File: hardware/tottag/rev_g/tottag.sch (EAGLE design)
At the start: 193 parts, among them J1 USB4110-GF-A, J2 DM3AT-SF-PEJM5, J3 TC2030-JLINK-NL-2SIDE, J4 TC2030-JLINK-NL-2SIDE, J5 MOLEX-PICO-SPOX-3SIDE, Q1 CSD75207W15, Q4 CSD75207W15, T1 HHM1595A1, U1 DW1000, U10 STM32F091CC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

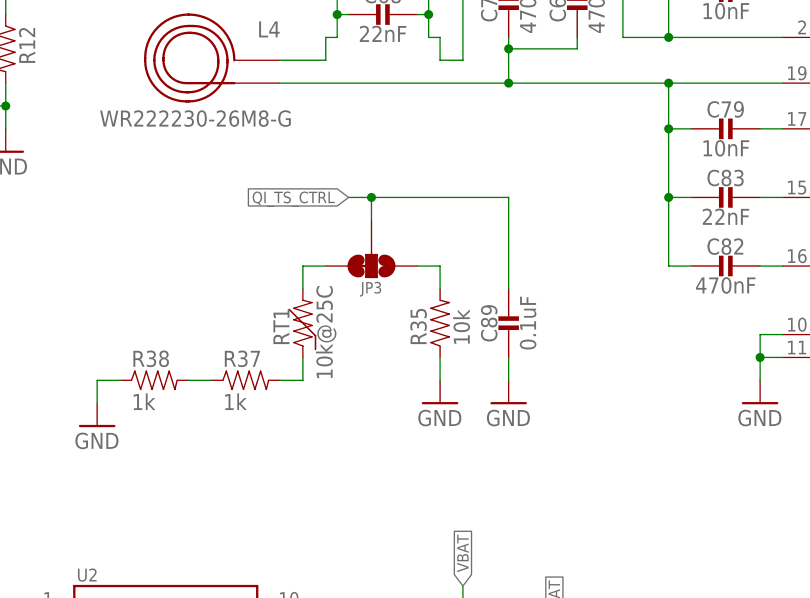
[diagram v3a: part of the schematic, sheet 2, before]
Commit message: rev_g: add more explanation of NTC math
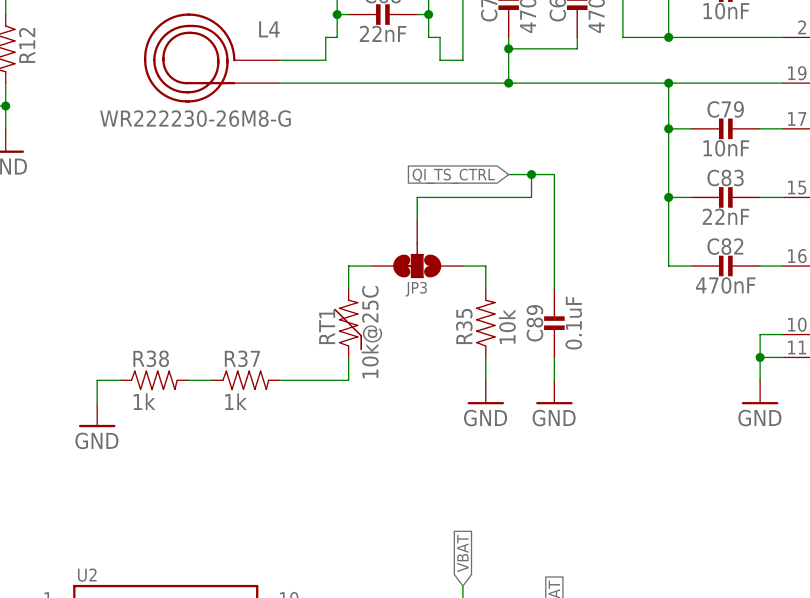
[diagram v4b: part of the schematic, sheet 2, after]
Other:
- note added: "Fig32 C3 No val given Guess small filter"
- note added: "Fig32 NTC"
- note added: "Fig32 R1"
- note added: "Reference: Datasheet §7.3.13 TS Resistor Network ---- Properties from the BQ51013B datasheet: Internal to chip (behind TS pad) is a 20kΩ pull-up to 2.2V On/off threshold V's are fixed, compute external R's V_HOT = 0.43V; external R of 28.5 kΩ V_COLD = 1.29V; external R of 4.9 kΩ ---- Thermistor datasheet values (where does it hit those R's?): 28.5kΩ @ 0.4ºC <-- this is good 4.9kΩ @ 44ºC <-- this 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"
- note removed: "Internal is 20kΩ pull-up to 2.2V V_HOT = 0.43V; eqiv 28.5kΩ V_COLD = 1.29V; eqiv 4.9kΩ ---- Thermistor values: 28.5kΩ @ 0.4ºC 4.9kΩ @ 44ºC ---- "Safe to touch" std says 60ºC 2.97kΩ @ 60ºC easy shift is add 2kΩ, now low 26.5kΩ @ 1.8ºC"
- moved on the sheet: C89, JP3, R35, RT1
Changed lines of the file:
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@@
 Need to - 2*97.6 = 328Ω</text>
 <wire x1="220.98" y1="129.54" x2="254" y2="129.54" width="0.1524" layer="98" style="longdash"/>
-<text x="109.982" y="144.018" size="0.8128" layer="98" align="top-left">This is a hedge.
+<text x="115.062" y="144.018" size="0.8128" layer="98" align="top-left">This is a hedge.
 Allow disabling thermal
 protection via solder jumper.</text>
-<wire x1="76.2" y1="116.84" x2="129.54" y2="116.84" width="0.127" layer="98" style="shortdash"/>
-<wire x1="76.2" y1="116.84" x2="76.2" y2="147.32" width="0.127" layer="98" style="shortdash"/>
-<text x="77.47" y="142.24" size="0.8128" layer="98" align="top-left">Internal is 20kΩ pull-up to 2.2V
-V_HOT = 0.43V; eqiv 28.5kΩ
-V_COLD = 1.29V; eqiv 4.9kΩ
+<wire x1="76.2" y1="116.84" x2="137.16" y2="116.84" width="0.127" layer="98" style="shortdash"/>
+<wire x1="76.2" y1="116.84" x2="76.2" y2="149.86" width="0.127" layer="98" style="shortdash"/>
+<text x="77.47" y="148.844" size="0.8128" layer="98" align="top-left">Reference: Datasheet §7.3.13 TS Resistor Network
 ----
-Thermistor values:
-28.5kΩ @ 0.4ºC
-4.9kΩ @ 44ºC
+Properties from the BQ51013B datasheet:
+Internal to chip (behind TS pad) is a 20kΩ pull-up to 2.2V
+On/off threshold V's are fixed, compute external R's
+V_HOT = 0.43V; external R of 28.5 kΩ
+V_COLD = 1.29V; external R of 4.9 kΩ
+----
+Thermistor datasheet values (where does it hit those R's?):
+28.5kΩ @ 0.4ºC &lt;-- this is good
+4.9kΩ @ 44ºC &lt;-- this is too low
 ----
 "Safe to touch" std says 60ºC
-2.97kΩ @ 60ºC
-easy shift is add 2kΩ, now low
-26.5kΩ @ 1.8ºC
-</text>
-<wire x1="76.2" y1="147.32" x2="129.54" y2="147.32" width="0.127" layer="98" style="shortdash"/>
-<wire x1="129.54" y1="116.84" x2="129.54" y2="147.32" width="0.127" layer="98" style="shortdash"/>
+NTC is 2.97kΩ @ 60ºC
+easy shift is add 2kΩ offset to NTC
+now V_COLD trips when NTC is 26.5kΩ (1.8ºC)</text>
+<wire x1="76.2" y1="149.86" x2="137.16" y2="149.86" width="0.127" layer="98" style="shortdash"/>
+<wire x1="137.16" y1="116.84" x2="137.16" y2="149.86" width="0.127" layer="98" style="shortdash"/>
 <text x="74.93" y="68.58" size="0.8128" layer="98" align="top-left">Datasheet wants a 10k NTC B=3370
 Battery pack has a 10k NTC B=3435
@@
 Power
 Switch</text>
+<text x="133.35" y="136.144" size="0.8128" layer="98" align="top-left">Fig32
+C3
+No val
+given
+Guess
+small
+filter</text>
+<text x="110.744" y="128.27" size="0.8128" layer="98" rot="R90" align="top-left">Fig32 NTC</text>
+<text x="87.122" y="122.174" size="0.8128" layer="98" align="top-left">Fig32 R1</text>
+<wire x1="97.79" y1="128.27" x2="82.55" y2="128.27" width="0.127" layer="98" style="shortdash"/>
+<wire x1="82.55" y1="128.27" x2="82.55" y2="120.65" width="0.127" layer="98" style="shortdash"/>
+<wire x1="97.79" y1="128.27" x2="97.79" y2="120.65" width="0.127" layer="98" style="shortdash"/>
+<wire x1="97.79" y1="120.65" x2="82.55" y2="120.65" width="0.127" layer="98" style="shortdash"/>
 </plain>
 <instances>
@@
 <attribute name="VALUE" x="226.06" y="162.56" size="1.778" layer="96"/>
 </instance>
-<instance part="JP3" gate="G$1" x="109.22" y="137.16" smashed="yes" rot="R270">
-<attribute name="NAME" x="109.22" y="135.382" size="1.27" layer="95" font="vector" ratio="12" align="top-center"/>
-</instance>
-<instance part="R35" gate="G$1" x="116.84" y="132.08" smashed="yes" rot="R90">
-<attribute name="DIGIKEY" x="116.84" y="132.08" size="1.778" layer="96" rot="R90" display="off"/>
-<attribute name="MPN" x="116.84" y="132.08" size="1.778" layer="96" rot="R90" display="off"/>
-<attribute name="NAME" x="115.3414" y="128.27" size="1.778" layer="95" rot="R90"/>
-<attribute name="VALUE" x="120.142" y="128.27" size="1.778" layer="96" rot="R90"/>
-</instance>
-<instance part="SUPPLY37" gate="1" x="116.84" y="121.92" smashed="yes">
-<attribute name="VALUE" x="114.3" y="119.38" size="1.778" layer="96"/>
-</instance>
-<instance part="RT1" gate="B" x="101.6" y="132.08" smashed="yes" rot="R90">
-<attribute name="NAME" x="100.1014" y="128.27" size="1.778" layer="95" rot="R90"/>
-<attribute name="VALUE" x="104.902" y="124.46" size="1.778" layer="96" rot="R90"/>
+<instance part="JP3" gate="G$1" x="114.3" y="137.16" smashed="yes" rot="R270">
+<attribute name="NAME" x="114.3" y="135.382" size="1.27" layer="95" font="vector" ratio="12" align="top-center"/>
+</instance>
+<instance part="R35" gate="G$1" x="121.92" y="132.08" smashed="yes" rot="R90">
+<attribute name="DIGIKEY" x="121.92" y="132.08" size="1.778" layer="96" rot="R90" display="off"/>
+<attribute name="MPN" x="121.92" y="132.08" size="1.778" layer="96" rot="R90" display="off"/>
+<attribute name="NAME" x="120.4214" y="128.27" size="1.778" layer="95" rot="R90"/>
+<attribute name="VALUE" x="125.222" y="128.27" size="1.778" layer="96" rot="R90"/>
+</instance>
+<instance part="SUPPLY37" gate="1" x="121.92" y="121.92" smashed="yes">
+<attribute name="VALUE" x="119.38" y="119.38" size="1.778" layer="96"/>
+</instance>
+<instance part="RT1" gate="B" x="106.68" y="132.08" smashed="yes" rot="R90">
+<attribute name="NAME" x="105.1814" y="128.27" size="1.778" layer="95" rot="R90"/>
+<attribute name="VALUE" x="109.982" y="124.46" size="1.778" layer="96" rot="R90"/>
 </instance>
 <instance part="SUPPLY38" gate="1" x="78.74" y="119.38" smashed="yes">
 <attribute name="VALUE" x="76.2" y="116.84" size="1.778" layer="96"/>
 </instance>
-<instance part="C89" gate="G$1" x="124.46" y="132.08" smashed="yes">
-<attribute name="DIGIKEY" x="124.46" y="132.08" size="1.778" layer="96" display="off"/>
-<attribute name="MPN" x="124.46" y="132.08" size="1.778" layer="96" display="off"/>
-<attribute name="NAME" x="123.19" y="130.81" size="1.778" layer="95" ratio="12" rot="R90" align="bottom-center"/>
-<attribute name="VALUE" x="125.73" y="130.81" size="1.778" layer="96" ratio="12" rot="R270" align="bottom-center"/>
-</instance>
-<instance part="SUPPLY39" gate="1" x="124.46" y="121.92" smashed="yes">
-<attribute name="VALUE" x="121.92" y="119.38" size="1.778" layer="96"/>
+<instance part="C89" gate="G$1" x="129.54" y="132.08" smashed="yes">
+<attribute name="DIGIKEY" x="129.54" y="132.08" size="1.778" layer="96" display="off"/>
+<attribute name="MPN" x="129.54" y="132.08" size="1.778" layer="96" display="off"/>
+<attribute name="NAME" x="128.27" y="130.81" size="1.778" layer="95" ratio="12" rot="R90" align="bottom-center"/>
+<attribute name="VALUE" x="130.81" y="130.81" size="1.778" layer="96" ratio="12" rot="R270" align="bottom-center"/>
+</instance>
+<instance part="SUPPLY39" gate="1" x="129.54" y="121.92" smashed="yes">
+<attribute name="VALUE" x="127" y="119.38" size="1.778" layer="96"/>
 </instance>
 <instance part="R37" gate="G$1" x="96.52" y="124.46" smashed="yes">
@@
 <pinref part="SUPPLY37" gate="1" pin="GND"/>
 <pinref part="R35" gate="G$1" pin="1"/>
-<wire x1="116.84" y1="127" x2="116.84" y2="124.46" width="0.1524" layer="91"/>
+<wire x1="121.92" y1="127" x2="121.92" y2="124.46" width="0.1524" layer="91"/>
 </segment>
 <segment>
 <pinref part="C89" gate="G$1" pin="2"/>
 <pinref part="SUPPLY39" gate="1" pin="GND"/>
-<wire x1="124.46" y1="127" x2="124.46" y2="124.46" width="0.1524" layer="91"/>
+<wire x1="129.54" y1="127" x2="129.54" y2="124.46" width="0.1524" layer="91"/>
 </segment>
 <segment>
@@
 <segment>
 <pinref part="JP3" gate="G$1" pin="2"/>
-<wire x1="109.22" y1="142.24" x2="109.22" y2="144.78" width="0.1524" layer="91"/>
-<wire x1="109.22" y1="144.78" x2="106.68" y2="144.78" width="0.1524" layer="91"/>
-<label x="106.68" y="144.78" size="1.27" layer="95" rot="R180" xref="yes"/>
+<wire x1="114.3" y1="142.24" x2="114.3" y2="144.78" width="0.1524" layer="91"/>
+<wire x1="114.3" y1="144.78" x2="127" y2="144.78" width="0.1524" layer="91"/>
+<wire x1="127" y1="144.78" x2="127" y2="147.32" width="0.1524" layer="91"/>
+<wire x1="127" y1="147.32" x2="124.46" y2="147.32" width="0.1524" layer="91"/>
+<label x="124.46" y="147.32" size="1.27" layer="95" rot="R180" xref="yes"/>
 <pinref part="C89" gate="G$1" pin="1"/>
-<wire x1="109.22" y1="144.78" x2="124.46" y2="144.78" width="0.1524" layer="91"/>
-<wire x1="124.46" y1="144.78" x2="124.46" y2="134.62" width="0.1524" layer="91"/>
-<junction x="109.22" y="144.78"/>
+<wire x1="127" y1="147.32" x2="129.54" y2="147.32" width="0.1524" layer="91"/>
+<wire x1="129.54" y1="147.32" x2="129.54" y2="134.62" width="0.1524" layer="91"/>
+<junction x="127" y="147.32"/>
 </segment>
 </net>
@@
 <segment>
 <pinref part="R35" gate="G$1" pin="2"/>
-<wire x1="116.84" y1="134.62" x2="116.84" y2="137.16" width="0.1524" layer="91"/>
-<wire x1="116.84" y1="137.16" x2="114.3" y2="137.16" width="0.1524" layer="91"/>
+<wire x1="121.92" y1="134.62" x2="121.92" y2="137.16" width="0.1524" layer="91"/>
+<wire x1="121.92" y1="137.16" x2="119.38" y2="137.16" width="0.1524" layer="91"/>
 <pinref part="JP3" gate="G$1" pin="1"/>
 </segment>
@@
 <pinref part="JP3" gate="G$1" pin="3"/>
 <pinref part="RT1" gate="B" pin="2"/>
-<wire x1="104.14" y1="137.16" x2="101.6" y2="137.16" width="0.1524" layer="91"/>
-<wire x1="101.6" y1="137.16" x2="101.6" y2="134.62" width="0.1524" layer="91"/>
+<wire x1="109.22" y1="137.16" x2="106.68" y2="137.16" width="0.1524" layer="91"/>
+<wire x1="106.68" y1="137.16" x2="106.68" y2="134.62" width="0.1524" layer="91"/>
 </segment>
 </net>
@@
 <pinref part="RT1" gate="B" pin="1"/>
 <pinref part="R37" gate="G$1" pin="2"/>
-<wire x1="101.6" y1="127" x2="101.6" y2="124.46" width="0.1524" layer="91"/>
-<wire x1="101.6" y1="124.46" x2="99.06" y2="124.46" width="0.1524" layer="91"/>
-</segment>
-</net>
+<wire x1="106.68" y1="127" x2="106.68" y2="124.46" width="0.1524" layer="91"/>
+<wire x1="106.68" y1="124.46" x2="99.06" y2="124.46" width="0.1524" layer="91"/>
+</segment>
+</net>

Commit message: rev_g: add more current control documentation
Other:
- note added: "Current control is a bit redundant here as VQI feeds directly to BQ24040, which also limits current. (Note that the BQ24040 is the more important limiter, as it limits from both USB and this source). Battery charge configured to max of 240 mA charge * 1.2 preterm = 288 mA. --- For simplicity, configure this to match the current limit of USB: 500 mA. This is comfortably more than the downstream li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"
- note added: "ISET controls constant charge current Battery wants 0.2C * 1200 mAh = 240 mA §9.2.1.2.1.1 Eqn R_ISET = [540AΩ/0.24A] = 2.25kΩ"
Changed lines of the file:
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@@
 <wire x1="97.79" y1="128.27" x2="97.79" y2="120.65" width="0.127" layer="98" style="shortdash"/>
 <wire x1="97.79" y1="120.65" x2="82.55" y2="120.65" width="0.127" layer="98" style="shortdash"/>
+<text x="39.37" y="63.5" size="0.8128" layer="98" align="top-left">ISET controls constant charge current
+Battery wants 0.2C * 1200 mAh = 240 mA
+§9.2.1.2.1.1 Eqn
+R_ISET = [540AΩ/0.24A] = 2.25kΩ</text>
+<text x="233.68" y="159.004" size="0.8128" layer="98">Current control is a bit redundant
+here as VQI feeds directly to BQ24040,
+which also limits current.
+(Note that the BQ24040 is the more
+important limiter, as it limits from
+both USB and this source).
+Battery charge configured to max of
+240 mA charge * 1.2 preterm = 288 mA.
+---
+For simplicity, configure this to match
+the current limit of USB: 500 mA.
+This is comfortably more than the
+downstream limit.</text>
+<wire x1="233.172" y1="158.75" x2="181.61" y2="147.574" width="0.0508" layer="98" style="shortdash"/>
 </plain>
 <instances>

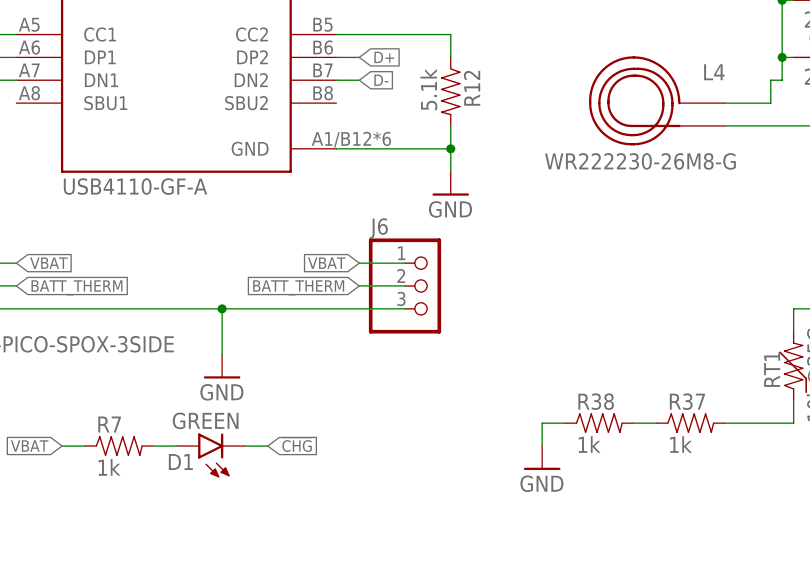
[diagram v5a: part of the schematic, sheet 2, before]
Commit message: rev_g: [WIP] design review fixes
 - Replace battery pinheader with individual pieces (allows U4 move later)
 - Fix lost ground plane (?!)
 - Then isolate and stitch up wireless ground plane to primary ground plane
 - Move routing from layer 2 to 15 where trivial to do so
 - Clean up C15 / C26 / C58 caps
 - Separate SD card passives from DW cap bank
 - Align R28
 - Add more vias around 3v3 / 1v8 conversion
 - Move U4 regulator farther from DW; add line of shield vias
 - Several plane cleanups with old route-arounds removed
 - Clean up some silk overlap errors
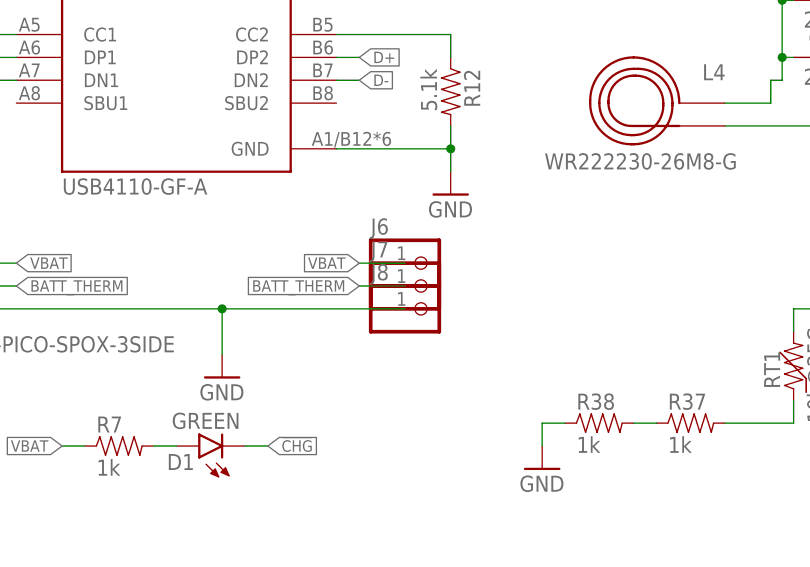
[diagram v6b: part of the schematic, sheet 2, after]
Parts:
- added J7, J8: (no value), pinhead:PINHD-1X1
- J6: device pinhead:PINHD-1X3 -> pinhead:PINHD-1X1
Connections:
- net BATT_THERM: now also J7.1; no longer J6.2
- net GND: now also J8.1; no longer J6.3
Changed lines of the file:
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@@
 <attribute name="MPN" value="CDSQR400B-HF"/>
 </part>
-<part name="J6" library="pinhead" library_urn="urn:adsk.eagle:library:325" deviceset="PINHD-1X3" device="" package3d_urn="urn:adsk.eagle:package:22458/2"/>
 <part name="R14" library="passives" deviceset="RESISTOR" device="0402_RES" value="100k"/>
 <part name="C75" library="passives" deviceset="CAPACITOR" device="0402_CAP" value="1uF">
@@
 <attribute name="MPN" value="GRM155R70G105KA12D "/>
 </part>
+<part name="J6" library="pinhead" library_urn="urn:adsk.eagle:library:325" deviceset="PINHD-1X1" device="" package3d_urn="urn:adsk.eagle:package:22485/2"/>
+<part name="J7" library="pinhead" library_urn="urn:adsk.eagle:library:325" deviceset="PINHD-1X1" device="" package3d_urn="urn:adsk.eagle:package:22485/2"/>
+<part name="J8" library="pinhead" library_urn="urn:adsk.eagle:library:325" deviceset="PINHD-1X1" device="" package3d_urn="urn:adsk.eagle:package:22485/2"/>
 </parts>
 <sheets>
@@
 <attribute name="VALUE" x="82.55" y="121.158" size="1.778" layer="96"/>
 </instance>
-<instance part="J6" gate="A" x="66.04" y="139.7" smashed="yes">
-<attribute name="NAME" x="59.69" y="145.415" size="1.778" layer="95"/>
-<attribute name="VALUE" x="59.69" y="132.08" size="1.778" layer="96"/>
-</instance>
 <instance part="C75" gate="G$1" x="43.18" y="93.98" smashed="yes">
 <attribute name="DIGIKEY" x="43.18" y="93.98" size="1.778" layer="96" display="off"/>
@@
 <attribute name="VALUE" x="120.65" y="92.71" size="1.778" layer="96" ratio="12" rot="R270" align="bottom-center"/>
 </instance>
+<instance part="J6" gate="G$1" x="66.04" y="142.24" smashed="yes">
+<attribute name="NAME" x="59.69" y="145.415" size="1.778" layer="95"/>
+<attribute name="VALUE" x="59.69" y="137.16" size="1.778" layer="96"/>
+</instance>
+<instance part="J7" gate="G$1" x="66.04" y="139.7" smashed="yes">
+<attribute name="NAME" x="59.69" y="142.875" size="1.778" layer="95"/>
+<attribute name="VALUE" x="59.69" y="134.62" size="1.778" layer="96"/>
+</instance>
+<instance part="J8" gate="G$1" x="66.04" y="137.16" smashed="yes">
+<attribute name="NAME" x="59.69" y="140.335" size="1.778" layer="95"/>
+<attribute name="VALUE" x="59.69" y="132.08" size="1.778" layer="96"/>
+</instance>
 </instances>
 <busses>
@@
 <wire x1="43.18" y1="137.16" x2="17.78" y2="137.16" width="0.1524" layer="91"/>
 <pinref part="J5" gate="G$1" pin="3"/>
-<pinref part="J6" gate="A" pin="3"/>
 <wire x1="63.5" y1="137.16" x2="43.18" y2="137.16" width="0.1524" layer="91"/>
 <junction x="43.18" y="137.16"/>
+<pinref part="J8" gate="G$1" pin="1"/>
 </segment>
 <segment>
@@
 </segment>
 <segment>
-<pinref part="J6" gate="A" pin="1"/>
 <wire x1="63.5" y1="142.24" x2="58.42" y2="142.24" width="0.1524" layer="91"/>
 <label x="58.42" y="142.24" size="1.27" layer="95" rot="R180" xref="yes"/>
+<pinref part="J6" gate="G$1" pin="1"/>
 </segment>
 </net>
@@
 </segment>
 <segment>
-<pinref part="J6" gate="A" pin="2"/>
 <wire x1="63.5" y1="139.7" x2="58.42" y2="139.7" width="0.1524" layer="91"/>
 <label x="58.42" y="139.7" size="1.27" layer="95" rot="R180" xref="yes"/>
-</segment>
-</net>
+<pinref part="J7" gate="G$1" pin="1"/>
+</segment>
+</net>

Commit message: rev_g: [WIP] design review fixes
 - add missing keepouts for bottom-left antenna
 - improve (increase) power connections around speaker parts
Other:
- note added: "BATTERY HCP643450NZC, 3.7V, 1200mah Bare raw cell: 6.4*34.5*50.5mm max. in T*W*L Assemble size: 6.4*34.5*52 mm max. in T*W*L Over-charge voltage: 4.28V Over- discharge voltage: 3.0V Continuous charge rate: 0.2C Peak charge rate:1C Continuous discharge rate: 0.2C Peak discharge rate:1C, for 2-3ms NTC, 10K B=3435 Wire: UL1571-28AWG#, 100mm, from left Connector: MOLEX87439-3P, positive PCM added"
- note removed: "BATTERY HCP643450NZC, 3.7V, 1200mah Bare raw cell: 6.4*34.5*50.5mm max. in T*W*L Assemble size: 6.4*34.5*52 mm max. in T*W*L Over-charge voltage: 4.28V Over- discharge voltage: 3.0V Continuous charge rate: 0.2C Peck charge rate:1C Continuous discharge rate: 0.2C Peck discharge rate:1C, for 2-3ms NTC, 10K B=3435 Wire: UL1571-28AWG#, 100mm, from left Connector: MOLEX87439-3P, positive PCM added"
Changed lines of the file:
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@@
 Over- discharge voltage: 3.0V
 Continuous charge rate: 0.2C
-Peck charge rate:1C
+Peak charge rate:1C
 Continuous discharge rate: 0.2C
-Peck discharge rate:1C, for 2-3ms
+Peak discharge rate:1C, for 2-3ms
 NTC, 10K B=3435
 Wire: UL1571-28AWG#, 100mm, from left

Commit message: rev_g: [WIP] Update BLE Antenna layout
 - Unsure about weird ground stub on reference drawing
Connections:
- net N$17 renamed BLE_ANT
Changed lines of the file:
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@@
 </segment>
 </net>
-<net name="N$17" class="0">
+<net name="BLE_ANT" class="0">
 <segment>
 <pinref part="L1" gate="G$1" pin="1"/>
